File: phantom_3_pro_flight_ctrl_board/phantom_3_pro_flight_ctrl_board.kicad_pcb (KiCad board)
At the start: 2 copper layers, 38 x 30 mm, 6 parts

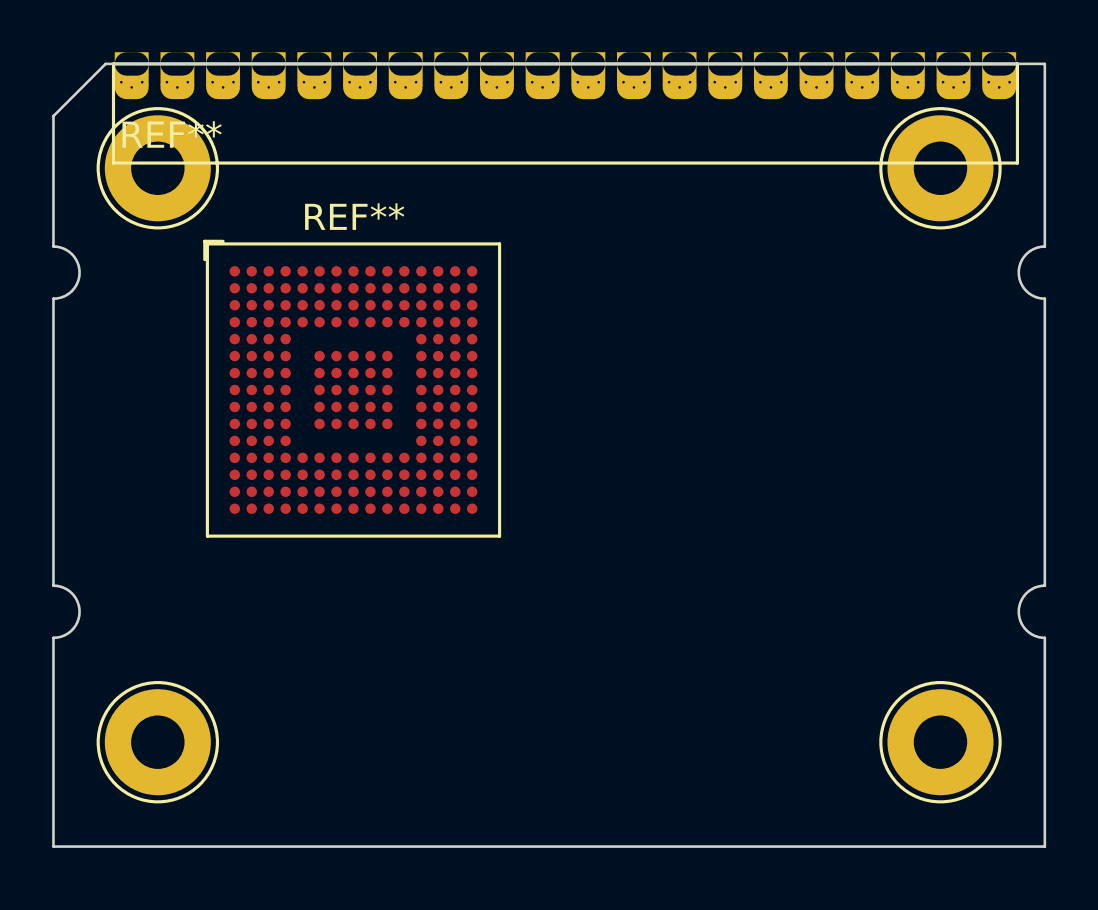
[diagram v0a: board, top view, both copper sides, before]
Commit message: Flight Ctrl: Updated uC component to map to BGA.
The microcontroller model was updated so that pin numbers map
to numbers in BGA footprint.

Also, edge pad connector footprints were updated.
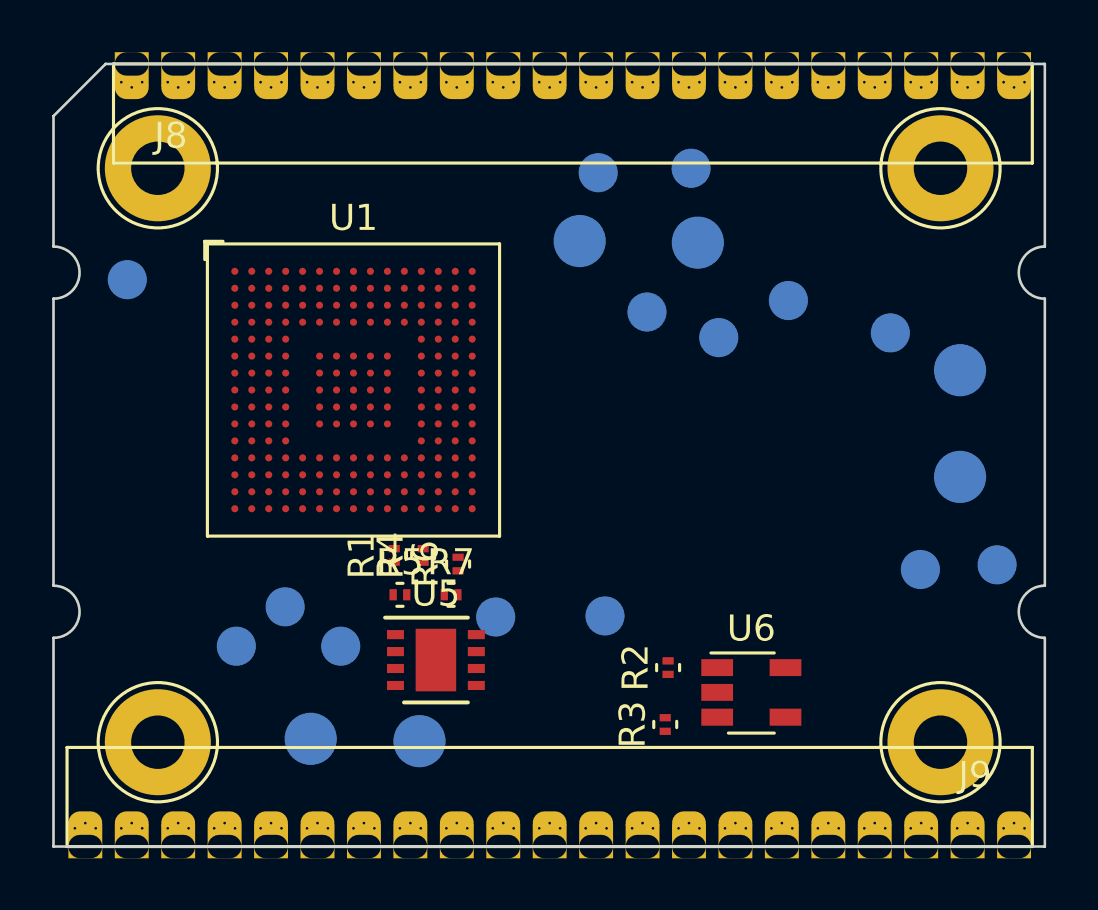
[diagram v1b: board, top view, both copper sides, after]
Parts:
- removed the REF** at (31.5, 32.5)
- removed the REF** at (23.0, 20.0)
- added J8: CONN_MC_FRONT, Connectors_custom:Connector-edge-20pin-1.78mm-cut, F.Cu at (23.0, 20.0)
- added J9: CONN_MC_BACK, Connectors_custom:Connector-edge-21pin-1.78mm-cut, F.Cu at (56.8, 50.0)
- added R1: 22Ω, Resistors_SMD:R_0201, F.Cu at (33.1, 38.8)
- added R2: 10kΩ, Resistors_SMD:R_0201, F.Cu at (43.6, 43.1)
- added R3: 15,7kΩ, Resistors_SMD:R_0201, F.Cu at (43.5, 45.3)
- added R4: 22Ω, Resistors_SMD:R_0201, F.Cu at (34.2, 38.8)
- added R5: 10kΩ, Resistors_SMD:R_0201, F.Cu at (33.3, 40.4)
- added R6: 100Ω, Resistors_SMD:R_0201, F.Cu at (35.5, 39.2)
- added R7: 10kΩ, Resistors_SMD:R_0201, F.Cu at (35.2, 40.4)
- added TP1: U3_RX, Measurement_Points:Measurement_Point_Round-SMD-Pad_Small, B.Cu at (40.9, 24.2)
- added TP10: SWDIO, Measurement_Points:Measurement_Point_Round-SMD-Pad_Small, B.Cu at (45.5, 30.5)
- added TP11: CAN1_R, Measurement_Points:Measurement_Point_Round-SMD-Pad_Big, B.Cu at (44.7, 26.9)
- added TP12: PB11, Measurement_Points:Measurement_Point_Round-SMD-Pad_Small, B.Cu at (41.1, 41.2)
- added TP13: VCC3V3, Measurement_Points:Measurement_Point_Round-SMD-Pad_Big, B.Cu at (34.0, 46.0)
- added TP14: PB10, Measurement_Points:Measurement_Point_Round-SMD-Pad_Small, B.Cu at (37.0, 41.2)
- added TP15: SWCLK, Measurement_Points:Measurement_Point_Round-SMD-Pad_Small, B.Cu at (42.8, 29.5)
- added TP16: GND, Measurement_Points:Measurement_Point_Round-SMD-Pad_Big, B.Cu at (29.9, 45.9)
- added TP17: GND, Measurement_Points:Measurement_Point_Round-SMD-Pad_Small, B.Cu at (31.0, 42.3)
- added TP18: GND, Measurement_Points:Measurement_Point_Round-SMD-Pad_Small, B.Cu at (48.2, 29.1)
- added TP19: DAC_OUT, Measurement_Points:Measurement_Point_Round-SMD-Pad_Small, B.Cu at (28.9, 40.8)
- added TP2: U3_TX, Measurement_Points:Measurement_Point_Round-SMD-Pad_Small, B.Cu at (44.4, 24.0)
- added TP20: 3V3A, Measurement_Points:Measurement_Point_Round-SMD-Pad_Small, B.Cu at (52.1, 30.3)
- added TP3: BOOT0, Measurement_Points:Measurement_Point_Round-SMD-Pad_Small, B.Cu at (22.8, 28.3)
- added TP4: GND, Measurement_Points:Measurement_Point_Round-SMD-Pad_Big, B.Cu at (54.8, 31.7)
- added TP5: 5V, Measurement_Points:Measurement_Point_Round-SMD-Pad_Big, B.Cu at (54.8, 35.8)
- added TP6: VCC3V6, Measurement_Points:Measurement_Point_Round-SMD-Pad_Small, B.Cu at (27.0, 42.3)
- added TP7: U7_RX, Measurement_Points:Measurement_Point_Round-SMD-Pad_Small, B.Cu at (53.2, 39.4)
- added TP8: U7_TX, Measurement_Points:Measurement_Point_Round-SMD-Pad_Small, B.Cu at (56.2, 39.2)
- added TP9: CAN1_T, Measurement_Points:Measurement_Point_Round-SMD-Pad_Big, B.Cu at (40.2, 26.8)
- added U1: STM32F427II, Housings_BGA_custom:BGA-176p25_10x10_11.0x11.0mm_Pitch0.65mm, F.Cu at (31.5, 32.5)
- added U5: PA 5xA, Housings_DFN_QFN:DFN-8-1EP_3x3mm_Pitch0.65mm, F.Cu at (34.7, 42.9)
- added U6: RC09, TO_SOT_Packages_SMD:TSOT-23-5, F.Cu at (46.8, 44.1)
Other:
- rule trace_min: 0.2 -> 0.12
- rule via_min_size: 0.4 -> 0.27

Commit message: Flight Ctrl: Added SD card and IMU.
The IMU is placed on separate board, but there are
footprints on the flight controller PCB to solder
it directly as well.
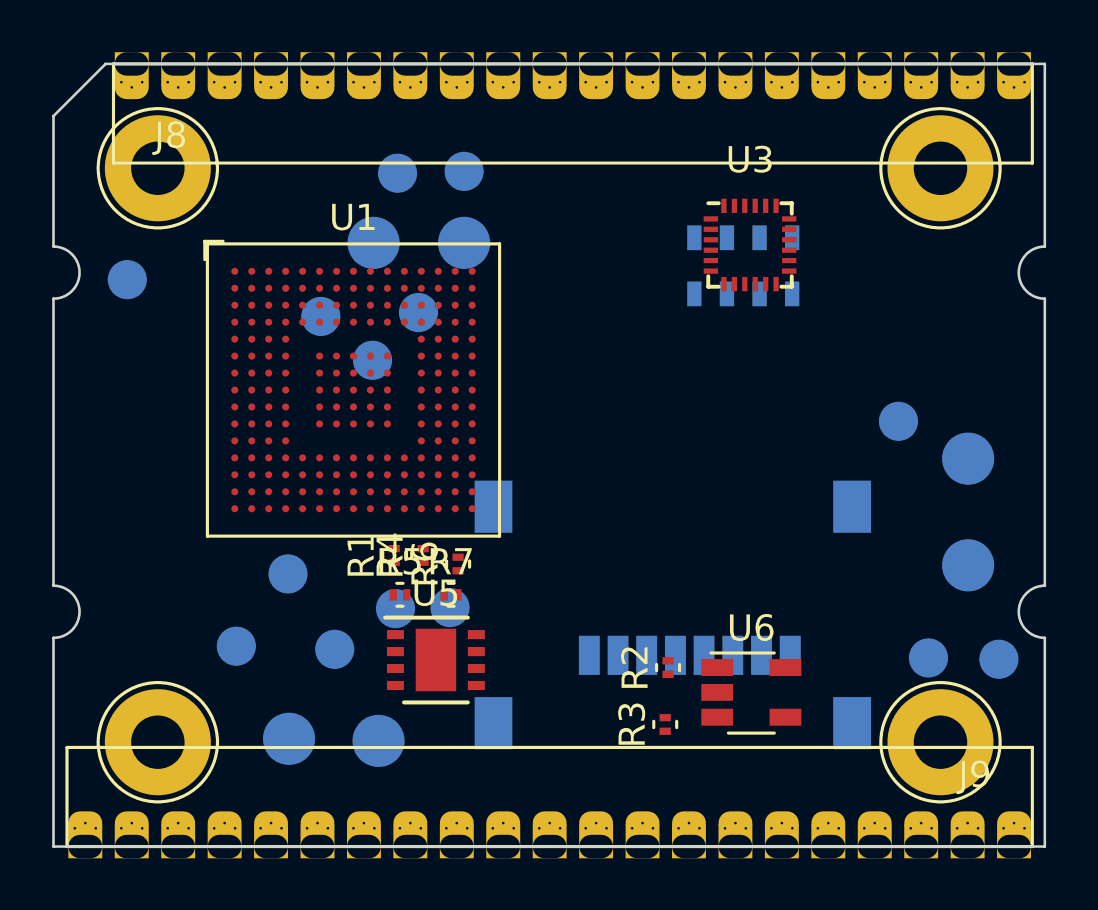
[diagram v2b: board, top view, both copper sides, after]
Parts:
- added J1: Micro_SD_Card, Connectors:microSD_Card_Receptacle_Wuerth_693072010801, B.Cu at (43.7, 40.0)
- added U2: MS5607, Housings_LGA:LGA-8_3x5mm_Pitch1.25mm, B.Cu at (46.4, 27.7)
- added U3: MPU-6500, Housings_DFN_QFN:QFN-24_3x3mm_Pitch0.4mm, F.Cu at (46.7, 26.9)
- moved TP18 14.2 mm to (34.0, 29.5)
- moved TP10 13.3 mm to (32.2, 31.4)
- moved TP15 12.5 mm to (30.2, 29.7)
- moved TP11 8.96 mm to (35.7, 26.9)
- moved TP2 8.70 mm to (35.7, 24.1)
- moved TP9 7.90 mm to (32.3, 26.9)
- moved TP1 7.69 mm to (33.2, 24.2)
- moved TP12 5.95 mm to (35.2, 40.8)
- moved TP14 3.85 mm to (33.1, 40.9)
- moved TP8 3.62 mm to (56.2, 42.8)
- moved TP20 3.40 mm to (52.4, 33.7)
- moved TP4 3.40 mm to (55.1, 35.1)
- moved TP5 3.40 mm to (55.1, 39.2)
- moved TP7 3.40 mm to (53.5, 42.8)
- moved TP13 1.57 mm to (32.5, 46.0)
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
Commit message: Flight Ctrl: Just renamed a symbol library, no real change.
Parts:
- U1: footprint Housings_BGA_custom:BGA-176p25_10x10_11.0x11.0mm_Pitch0.65mm -> Housings_BGA-v2:BGA-176p25_10x10_11.0x11.0mm_Pitch0.65mm
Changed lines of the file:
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@@
     (pad 1 thru_hole circle (at 0 0) (size 4.064 4.064) (drill 2.048) (layers *.Cu *.Mask))
   )
-  (module Housings_BGA_custom:BGA-176p25_10x10_11.0x11.0mm_Pitch0.65mm (layer F.Cu)
+  (module Housings_BGA-v2:BGA-176p25_10x10_11.0x11.0mm_Pitch0.65mm (layer F.Cu)
     (at 31.5 32.5)
     (descr "UFBGA225, TI uC")
